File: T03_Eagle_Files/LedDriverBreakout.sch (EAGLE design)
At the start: 3 parts, among them U1 TPS61161ADRVT, X1 22-23-2031, X2 22-23-2031

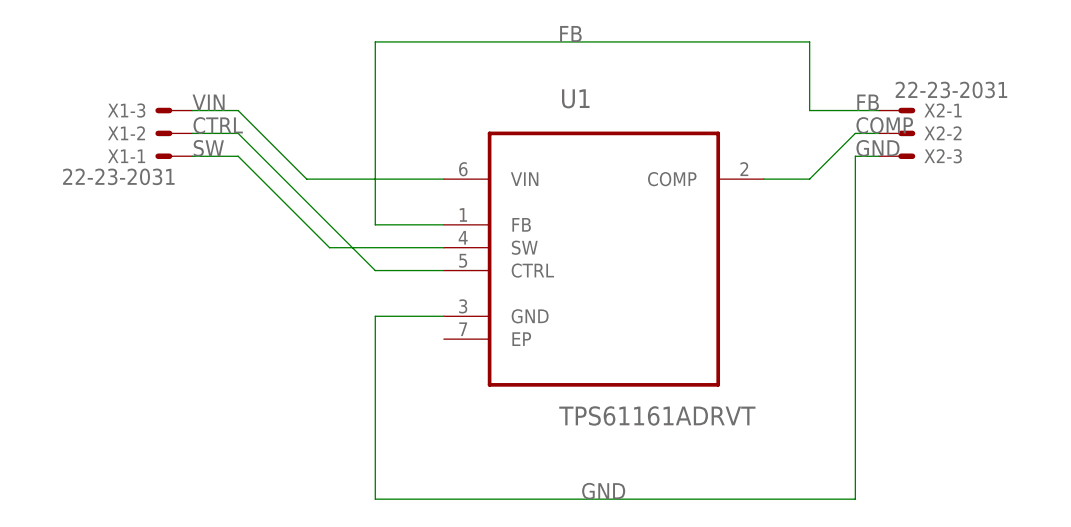
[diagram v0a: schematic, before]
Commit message: Cleaned up LED driver breakoout for machining
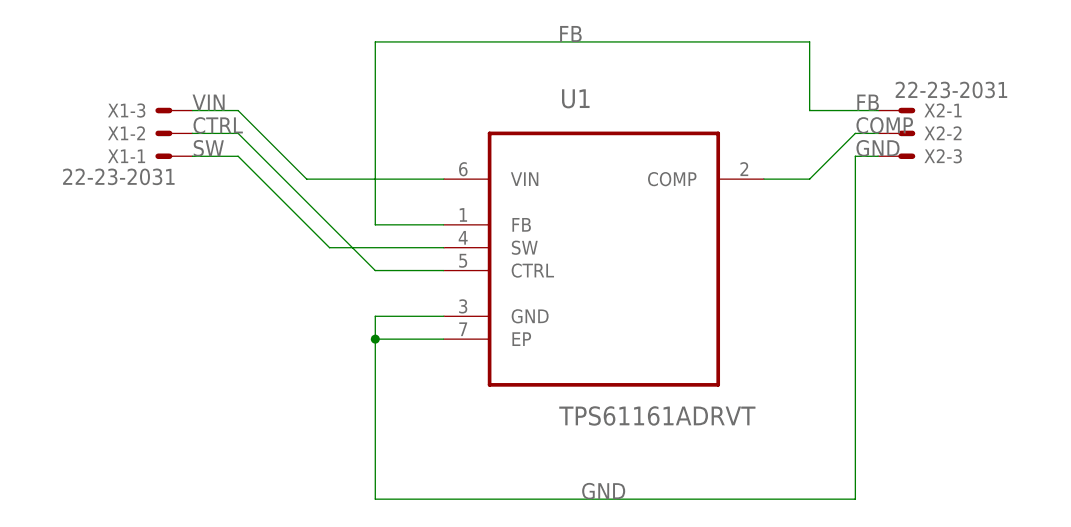
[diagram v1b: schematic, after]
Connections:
- net GND: now also U1.EP
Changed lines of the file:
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@@
 <?xml version="1.0" encoding="utf-8"?>
 <!DOCTYPE eagle SYSTEM "eagle.dtd">
-<eagle version="7.4.0">
+<eagle version="7.2.0">
 <drawing>
 <settings>
@@
 <pinref part="U1" gate="A" pin="GND"/>
 <wire x1="48.26" y1="45.72" x2="40.64" y2="45.72" width="0.1524" layer="91"/>
-<wire x1="40.64" y1="45.72" x2="40.64" y2="25.4" width="0.1524" layer="91"/>
+<wire x1="40.64" y1="45.72" x2="40.64" y2="43.18" width="0.1524" layer="91"/>
+<wire x1="40.64" y1="43.18" x2="40.64" y2="25.4" width="0.1524" layer="91"/>
 <wire x1="40.64" y1="25.4" x2="93.98" y2="25.4" width="0.1524" layer="91"/>
 <wire x1="93.98" y1="25.4" x2="93.98" y2="63.5" width="0.1524" layer="91"/>
@@
 <label x="63.5" y="25.4" size="1.778" layer="95"/>
 <label x="93.98" y="63.5" size="1.778" layer="95"/>
+<pinref part="U1" gate="A" pin="EP"/>
+<wire x1="48.26" y1="43.18" x2="40.64" y2="43.18" width="0.1524" layer="91"/>
+<junction x="40.64" y="43.18"/>
 </segment>
 </net>
